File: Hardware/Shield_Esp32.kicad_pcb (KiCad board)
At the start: 2 copper layers, 81.3 x 55.3 mm, 46 parts, among them J1 Conn_01x02_Male, J10 Conn_01x02_Male, J11 Conn_01x02_Male, J12 Conn_01x02_Male, J13 Conn_01x02_Male, J14 Conn_01x02_Male, J15 Conn_01x02_Male, J16 Conn_01x02_Male, J17 Conn_01x02_Male, J18 Conn_01x02_Male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

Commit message: update pcb
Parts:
- added R10: 10k, Resistor_SMD:R_0805_2012Metric, B.Cu at (186.9, 115.7)
- added R11: 10k, Resistor_SMD:R_0805_2012Metric, B.Cu at (179.0, 115.6)
- R3, R5: value 15k -> 18,7k
- moved J16 0.26 mm to (174.9, 120.8)
- moved J9 0.26 mm to (186.9, 120.8)
- moved J1 0.26 mm to (158.8, 120.7)
- moved J10 0.26 mm to (182.9, 120.7)
- moved J15 0.26 mm to (178.9, 120.7)
- moved J17 0.26 mm to (170.9, 120.7)
- moved J18 0.26 mm to (166.9, 120.7)
- moved J2 0.26 mm to (162.9, 120.7)
- moved J6 0.26 mm to (190.9, 120.7)
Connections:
- J15 pad 2: D14 -> Net-(J15-Pad2)
- J9 pad 2: D13 -> Net-(J9-Pad2)
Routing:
- net Net-(J15-Pad2): track 0.00 -> 2.94 mm
- net D13: track 9.51 -> 6.70 mm
- net Net-(J9-Pad2): track 0.00 -> 2.55 mm
- net D14: track 8.28 -> 6.09 mm
- net TRIG0: track 51.2 -> 52.0 mm

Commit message: fixed pcb
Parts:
- J3: moved to B.Cu
- moved J6 44.2 mm to (191.5, 76.5), turned to -90 degrees
- moved J3 3.25 mm to (138.6, 85.1), turned to 180 degrees
- moved J23 2.50 mm to (193.4, 83.2), turned to 180 degrees
- moved D4 1.23 mm to (194.8, 108.7)
- moved C2 0.12 mm to (188.0, 91.4)
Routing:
- net PWM2: track 115.6 -> 73.4 mm
- net ADC1: track 84.8 -> 44.6 mm, vias 0 -> 2
- net AMP1: track 88.8 -> 59.9 mm, vias 2 -> 0
- net TRIG0: track 52.0 -> 75.9 mm, vias 0 -> 2
- net TRIG1: track 57.2 -> 79.7 mm, vias 2 -> 0
- net PWM2N: track 92.7 -> 70.9 mm, vias 0 -> 2
- net PWM1N: track 57.2 -> 37.9 mm, vias 2 -> 0
- net D32: track 15.1 -> 32.7 mm
- net RXB: track 55.4 -> 38.2 mm
- net PWM1: track 69.7 -> 52.5 mm, vias 0 -> 2
- net R_TCRT: track 52.6 -> 69.0 mm
- net ADC0: track 69.8 -> 53.6 mm
- net ADC2: track 87.1 -> 71.4 mm
- net TXB: track 66.1 -> 50.6 mm, vias 2 -> 0
- net ECHO0: track 55.0 -> 70.3 mm, vias 0 -> 2
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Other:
- board text added: "ESP32 Buggy Shield v2"
- board text removed: "ESP32 Buggy Shield"

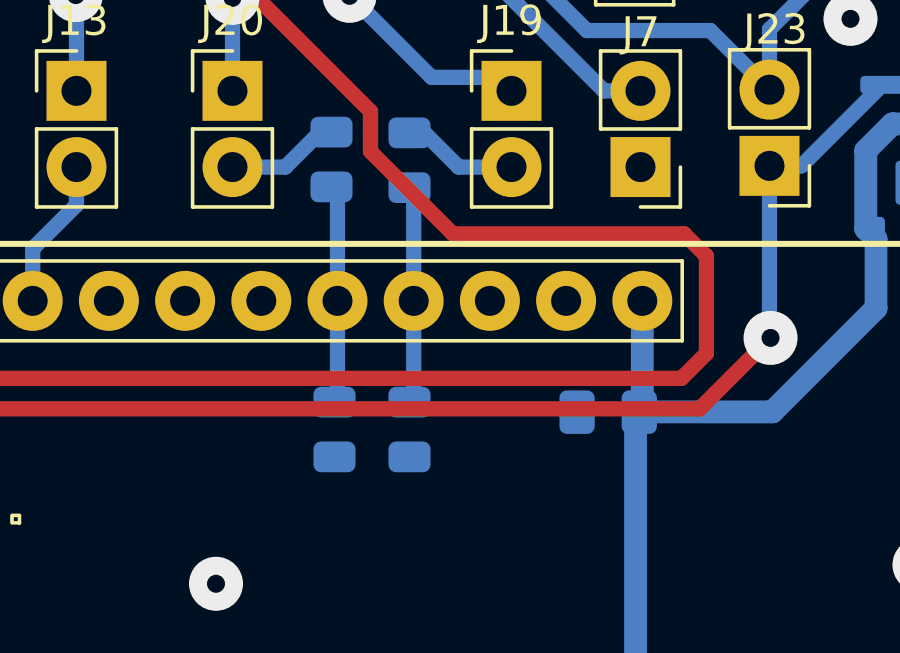
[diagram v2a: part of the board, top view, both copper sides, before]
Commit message: correção pino encoder
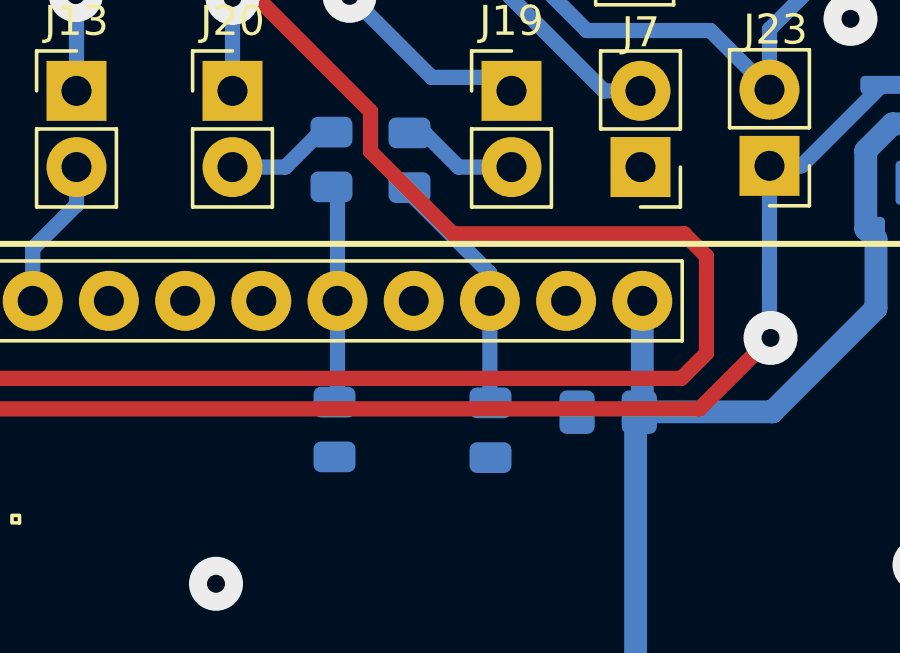
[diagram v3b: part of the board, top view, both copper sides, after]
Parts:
- R8, R9: value 15k -> 20k
- moved R8 2.70 mm to (184.1, 92.0)
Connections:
- J5 pad 12: D2 -> unconnected-(J5-Pad12)
- J5 pad 13: unconnected-(J5-Pad13) -> D15
- R6 pad 2: D2 -> D15
- R8 pad 1: D2 -> D15
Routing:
- net D15: track 0.00 -> 8.36 mm
- net D2: track 7.27 -> 0.00 mm
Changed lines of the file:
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@@
   (net 49 "unconnected-(J5-Pad10)")
   (net 50 "D4")
-  (net 51 "D2")
-  (net 52 "unconnected-(J5-Pad13)")
+  (net 51 "unconnected-(J5-Pad12)")
+  (net 52 "D15")
   (net 53 "Net-(J19-Pad2)")
   (net 54 "Net-(J20-Pad2)")
@@
       (net 50 "D4") (pinfunction "Pin_11") (pintype "passive"))
     (pad "12" thru_hole oval (at 0 27.94 90) (size 2 2) (drill 1) (layers *.Cu *.Mask)
-      (net 51 "D2") (pinfunction "Pin_12") (pintype "passive"))
+      (net 51 "unconnected-(J5-Pad12)") (pinfunction "Pin_12") (pintype "passive+no_connect"))
     (pad "13" thru_hole oval (at 0 30.48 90) (size 2 2) (drill 1) (layers *.Cu *.Mask)
-      (net 52 "unconnected-(J5-Pad13)") (pinfunction "Pin_13") (pintype "passive+no_connect"))
+      (net 52 "D15") (pinfunction "Pin_13") (pintype "passive"))
     (pad "14" thru_hole oval (at 0 33.02 90) (size 2 2) (drill 1) (layers *.Cu *.Mask)
       (net 2 "GND") (pinfunction "Pin_14") (pintype "passive"))
@@
   )
   (footprint "Resistor_SMD:R_0805_2012Metric" (layer "B.Cu")
-    (at 181.4 91.9875 -90)
+    (at 184.1 92.0125 -90)
     (descr "Resistor SMD 0805 (2012 Metric), square (rectangular) end terminal, IPC_7351 nominal, (Body size source: IPC-SM-782 page 72, https://www.pcb-3d.com/wordpress/wp-content/uploads/ipc-sm-782a_amendment_1_and_2.pdf), generated with kicad-footprint-generator")
     (tags "resistor")
@@
       (effects (font (size 1 1) (thickness 0.15)) (justify mirror))
     )
-    (fp_text value "15k" (at 0 -1.65 90) (layer "B.Fab")
+    (fp_text value "20k" (at 0 -1.65 90) (layer "B.Fab")
       (effects (font (size 1 1) (thickness 0.15)) (justify mirror))
     )
@@
     (fp_line (start -1 -0.625) (end -1 0.625) (layer "B.Fab") (width 0.1))
     (pad "1" smd roundrect (at -0.9125 0 270) (size 1.025 1.4) (layers "B.Cu" "B.Paste" "B.Mask") (roundrect_rratio 0.243902439)
-      (net 51 "D2") (pintype "passive"))
+      (net 52 "D15") (pintype "passive"))
     (pad "2" smd roundrect (at 0.9125 0 270) (size 1.025 1.4) (layers "B.Cu" "B.Paste" "B.Mask") (roundrect_rratio 0.243902439)
       (net 2 "GND") (pintype "passive"))
@@
       (effects (font (size 1 1) (thickness 0.15)) (justify mirror))
     )
-    (fp_text value "15k" (at 0 -1.65 90) (layer "B.Fab")
+    (fp_text value "20k" (at 0 -1.65 90) (layer "B.Fab")
       (effects (font (size 1 1) (thickness 0.15)) (justify mirror))
     )
@@
       (net 53 "Net-(J19-Pad2)") (pintype "passive"))
     (pad "2" smd roundrect (at 0.9125 0 270) (size 1.025 1.4) (layers "B.Cu" "B.Paste" "B.Mask") (roundrect_rratio 0.243902439)
-      (net 51 "D2") (pintype "passive"))
+      (net 52 "D15") (pintype "passive"))
     (model "${KICAD6_3DMODEL_DIR}/Resistor_SMD.3dshapes/R_0805_2012Metric.wrl"
       (offset (xyz 0 0 0))
@@
   (segment (start 178.8 83.9) (end 179 84.1) (width 0.508) (layer "B.Cu") (net 50))
   (segment (start 179 90.975) (end 179 87.7) (width 0.508) (layer "B.Cu") (net 50))
-  (segment (start 181.4 83.925) (end 181.54 84.065) (width 0.508) (layer "B.Cu") (net 51))
-  (segment (start 181.54 84.065) (end 181.54 87.7) (width 0.508) (layer "B.Cu") (net 51))
-  (segment (start 181.54 90.935) (end 181.54 87.7) (width 0.508) (layer "B.Cu") (net 51))
-  (segment (start 181.4 91.075) (end 181.54 90.935) (width 0.508) (layer "B.Cu") (net 51))
+  (segment (start 183.9 91.1) (end 184.08 90.92) (width 0.508) (layer "B.Cu") (net 52))
+  (segment (start 184.08 86.78) (end 181.4 84.1) (width 0.508) (layer "B.Cu") (net 52))
+  (segment (start 181.4 84.1) (end 181.4 83.925) (width 0.508) (layer "B.Cu") (net 52))
+  (segment (start 184.08 90.92) (end 184.08 87.7) (width 0.508) (layer "B.Cu") (net 52))
+  (segment (start 184.08 87.7) (end 184.08 86.78) (width 0.508) (layer "B.Cu") (net 52))
   (segment (start 181.4 82.1) (end 181.8979 82.1) (width 0.508) (layer "B.Cu") (net 53))
   (segment (start 184.8 83.24) (end 183.0379 83.24) (width 0.508) (layer "B.Cu") (net 53))
